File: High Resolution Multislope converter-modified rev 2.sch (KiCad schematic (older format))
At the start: 225 parts, among them J1 UART, J2 Input, J3 ICSP6, J4 ISCP10, J5 Power, Q1 BC856, Q2 BC847, Q3 BC856, Q4 BC856, Q5 BC856, Q6 BC856, Q7 BC847, Q8 BC847, Q9 BC856, U1 OPA172, U10 LM393, U11 OPA145, U12 OPA145, U13 MCP6002, U14 7815, U15 7915, U16 LTC2057, U17 74HC74, U18 OPA197, U19 OPA172, U2 OPA172, U20 DG419LDY, U202 MCP4921, U204 ADuM1201AR, U21 OP07CR, U3 7805, U4 NE5534D, U5 74LV4053, U6 LM399H, U7 DG408DJ, U8 OP07CR, U9 OP07CR, X1 16MHz

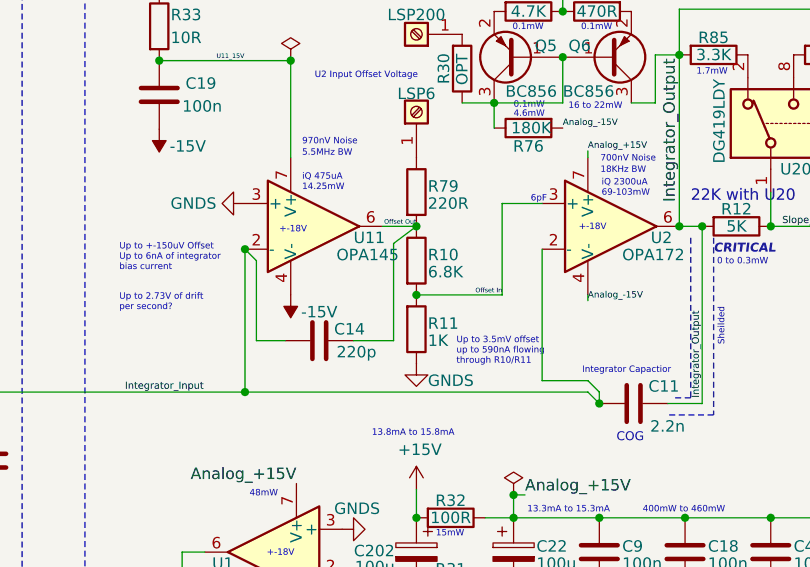
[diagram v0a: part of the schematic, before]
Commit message: Added silk screen descriptions
All test points and through hole points labeled on front and back

Added test points near to the reference to make it easier to add other references.
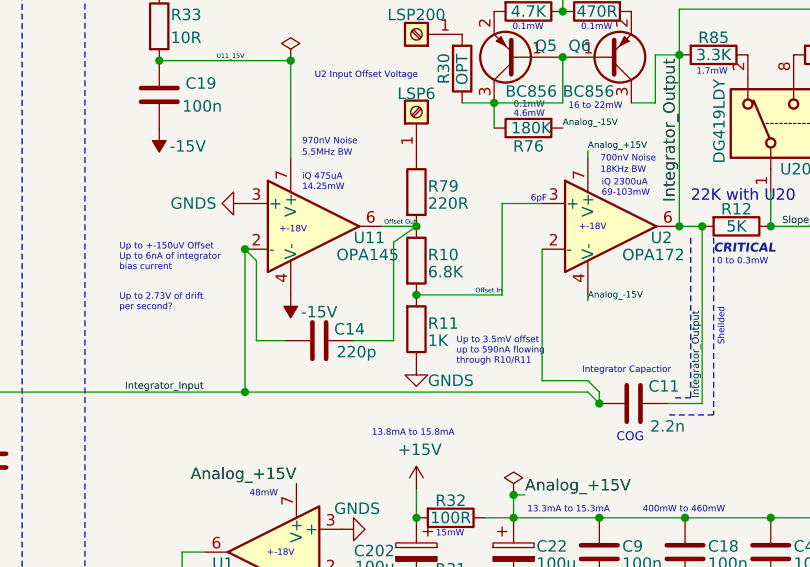
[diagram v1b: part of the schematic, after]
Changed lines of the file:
@@
 	10495 3075 10875 3075
 Wire Wire Line
-	10550 5425 10650 5350
+	10550 5420 10550 5850
 Wire Wire Line
-	10550 5850 10550 5425
+	10550 5420 10650 5350
 Wire Wire Line
 	10585 1860 10775 1860
